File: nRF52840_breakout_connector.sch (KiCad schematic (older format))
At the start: 4 parts, among them J2 Conn_02x03_Odd_Even, J3 Conn_01x22, J4 Conn_01x16, J5 Conn_01x22

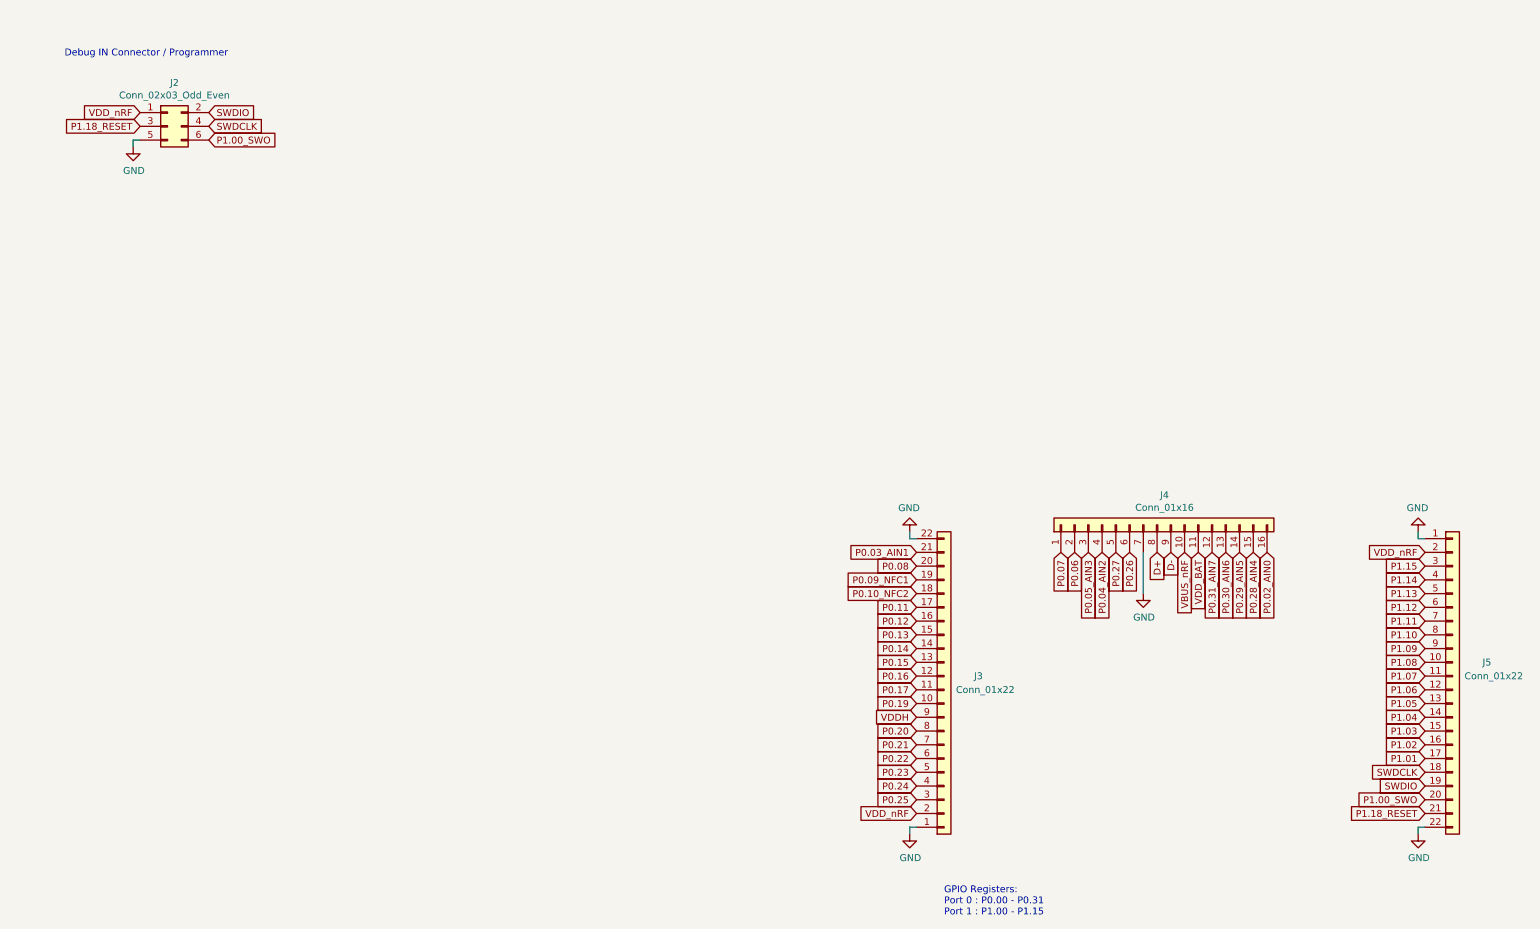
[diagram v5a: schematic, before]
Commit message: minor changes / switched from tag - 10pol debug connector
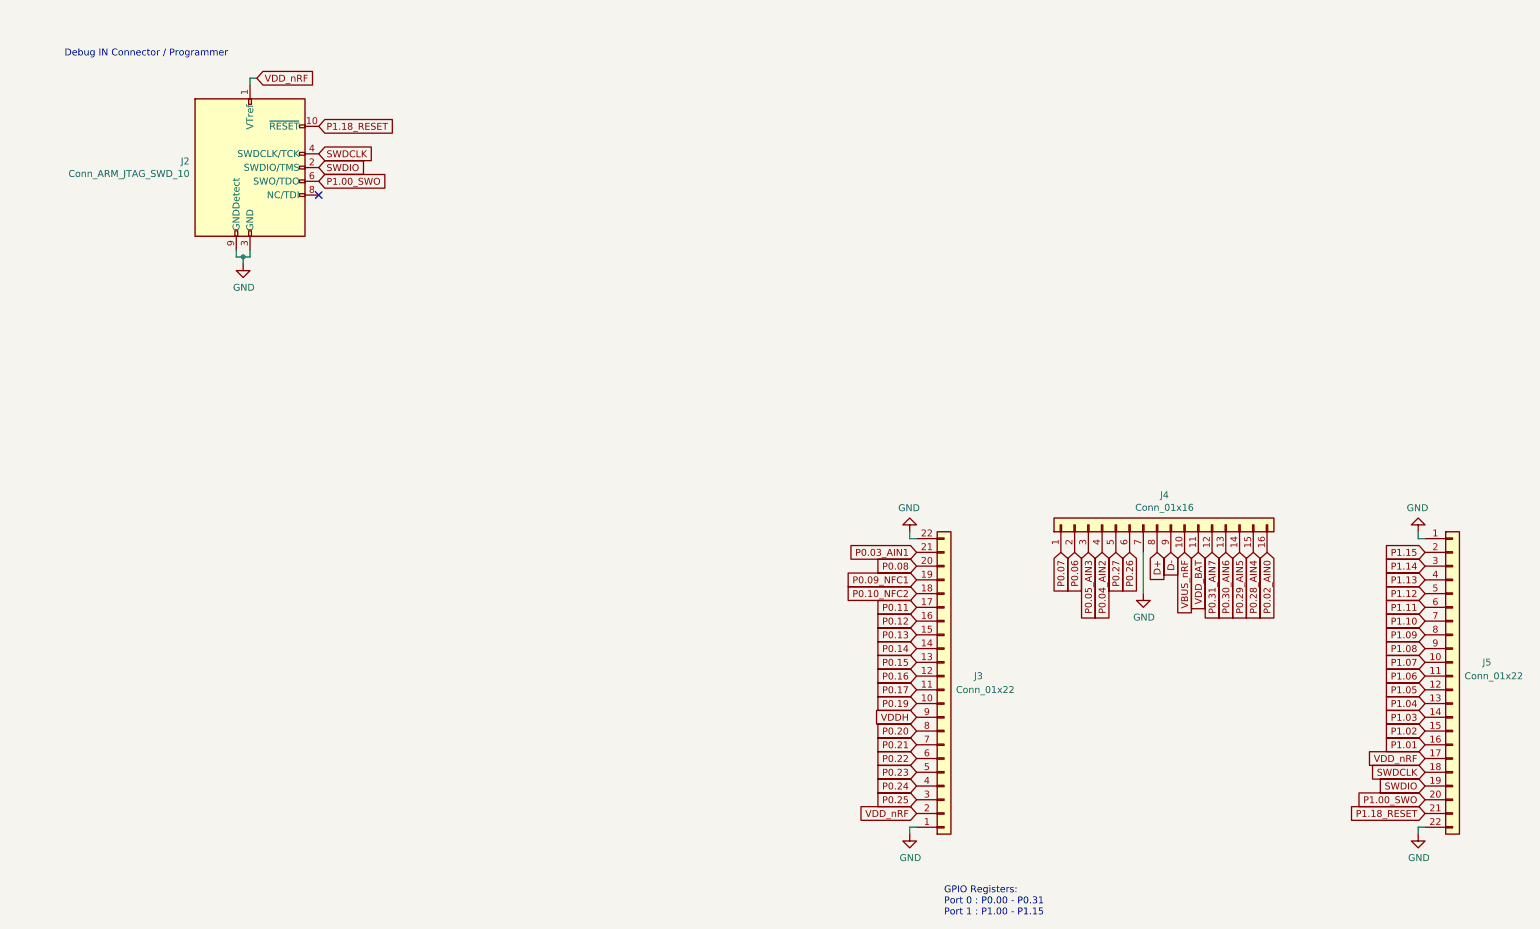
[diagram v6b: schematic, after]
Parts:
- removed J2: Conn_02x03_Odd_Even, Connector:Tag-Connect_TC2030-IDC-NL_2x03_P1.27mm_Vertical, symbol Connector_Generic:Conn_02x03_Odd_Even
- added J2: Conn_ARM_JTAG_SWD_10, Connector_PinHeader_1.27mm:PinHeader_2x05_P1.27mm_Vertical_SMD, symbol Connector:Conn_ARM_JTAG_SWD_10
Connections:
- net GND: now also J2.3 (GND), J2.5 (GND), J2.9 (GNDDetect)
- net P1.00_SWO: now also J2.6 (SWO/TDO)
- net P1.01: now also J5.16 (Pin_16); no longer J5.17 (Pin_17)
- net P1.02: now also J5.15 (Pin_15); no longer J5.16 (Pin_16)
- net P1.03: now also J5.14 (Pin_14); no longer J5.15 (Pin_15)
- net P1.04: now also J5.13 (Pin_13); no longer J5.14 (Pin_14)
- net P1.05: now also J5.12 (Pin_12); no longer J5.13 (Pin_13)
- net P1.06: now also J5.11 (Pin_11); no longer J5.12 (Pin_12)
- net P1.07: now also J5.10 (Pin_10); no longer J5.11 (Pin_11)
- net P1.08: now also J5.9 (Pin_9); no longer J5.10 (Pin_10)
- net P1.09: now also J5.8 (Pin_8); no longer J5.9 (Pin_9)
- net P1.10: now also J5.7 (Pin_7); no longer J5.8 (Pin_8)
- net P1.11: now also J5.6 (Pin_6); no longer J5.7 (Pin_7)
- net P1.12: now also J5.5 (Pin_5); no longer J5.6 (Pin_6)
- net P1.13: now also J5.4 (Pin_4); no longer J5.5 (Pin_5)
- net P1.14: now also J5.3 (Pin_3); no longer J5.4 (Pin_4)
- net P1.15: now also J5.2 (Pin_2); no longer J5.3 (Pin_3)
- net P1.18_RESET: now also J2.10 (~RESET~)
- net SWDCLK: now also J2.4 (SWDCLK/TCK)
- net SWDIO: now also J2.2 (SWDIO/TMS)
- net VDD_nRF: now also J5.17 (Pin_17), J2.1 (VTref); no longer J5.2 (Pin_2)
- no-connect marks 0 -> 1
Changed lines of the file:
@@
 Comment4 ""
 $EndDescr
-Text GLabel 1150 1000 0    50   Input ~ 0
-VDD_nRF
-$Comp
-L power:GND #PWR?
-U 1 1 5C9538B5
-P 1100 1250
-AR Path="/5C9538B5" Ref="#PWR?"  Part="1"
-AR Path="/5C94F379/5C9538B5" Ref="#PWR020"  Part="1"
-F 0 "#PWR020" H 1100 1000 50  0001 C CNN
-F 1 "GND" H 1105 1077 50  0000 C CNN
-F 2 "" H 1100 1250 50  0001 C CNN
-F 3 "" H 1100 1250 50  0001 C CNN
-	1    1100 1250
-	1    0    0    -1
-$EndComp
-Text GLabel 1650 1000 2    50   Input ~ 0
-SWDIO
-Text GLabel 1650 1100 2    50   Input ~ 0
-SWDCLK
 Text Notes 600  600  0    50   ~ 0
 Debug IN Connector / Programmer
@@
 Text GLabel 6800 4600 0    50   Input ~ 0
 P0.11
+Text GLabel 10500 4800 0    50   Input ~ 0
+P1.09
 Text GLabel 10500 4900 0    50   Input ~ 0
-P1.09
-Text GLabel 10500 5000 0    50   Input ~ 0
 P1.08
 Text GLabel 6800 4300 0    50   Input ~ 0
@@
 Text GLabel 10500 6000 0    50   Input ~ 0
 P1.00_SWO
-Text GLabel 10500 4600 0    50   Input ~ 0
+Text GLabel 10500 4500 0    50   Input ~ 0
 P1.12
-Text GLabel 10500 4500 0    50   Input ~ 0
+Text GLabel 10500 4400 0    50   Input ~ 0
 P1.13
-Text GLabel 10500 4400 0    50   Input ~ 0
+Text GLabel 10500 4300 0    50   Input ~ 0
 P1.14
-Text GLabel 10500 4300 0    50   Input ~ 0
+Text GLabel 10500 4200 0    50   Input ~ 0
 P1.15
 Text GLabel 6800 4200 0    50   Input ~ 0
@@
 Text GLabel 8950 4200 3    50   Input ~ 0
 P0.31_AIN7
-Text GLabel 10500 4800 0    50   Input ~ 0
+Text GLabel 10500 4700 0    50   Input ~ 0
 P1.10
-Text GLabel 10500 4700 0    50   Input ~ 0
+Text GLabel 10500 4600 0    50   Input ~ 0
 P1.11
 Text GLabel 6800 4500 0    50   Input ~ 0
@@
 Text GLabel 10500 5800 0    50   Input ~ 0
 SWDCLK
-Text GLabel 10500 5700 0    50   Input ~ 0
+Text GLabel 10500 5600 0    50   Input ~ 0
 P1.01
-Text GLabel 10500 5600 0    50   Input ~ 0
+Text GLabel 10500 5500 0    50   Input ~ 0
 P1.02
-Text GLabel 10500 5500 0    50   Input ~ 0
+Text GLabel 10500 5400 0    50   Input ~ 0
 P1.03
-Text GLabel 10500 5400 0    50   Input ~ 0
+Text GLabel 10500 5300 0    50   Input ~ 0
 P1.04
-Text GLabel 10500 5300 0    50   Input ~ 0
+Text GLabel 10500 5200 0    50   Input ~ 0
 P1.05
-Text GLabel 10500 5200 0    50   Input ~ 0
+Text GLabel 10500 5100 0    50   Input ~ 0
 P1.06
-Text GLabel 10500 5100 0    50   Input ~ 0
+Text GLabel 10500 5000 0    50   Input ~ 0
 P1.07
 Text GLabel 8850 4200 3    50   Input ~ 0
@@
 Wire Wire Line
 	6750 6200 6800 6200
-Text GLabel 10500 4200 0    50   Input ~ 0
+Text GLabel 10500 5700 0    50   Input ~ 0
 VDD_nRF
 $Comp
@@
 $EndComp
 $Comp
-L Connector_Generic:Conn_02x03_Odd_Even J2
-U 1 1 5CC7EB10
-P 1350 1100
-F 0 "J2" H 1400 1417 50  0000 C CNN
-F 1 "Conn_02x03_Odd_Even" H 1400 1326 50  0000 C CNN
-F 2 "Connector:Tag-Connect_TC2030-IDC-NL_2x03_P1.27mm_Vertical" H 1350 1100 50  0001 C CNN
-F 3 "~" H 1350 1100 50  0001 C CNN
-	1    1350 1100
-	1    0    0    -1
-$EndComp
-Text GLabel 1650 1200 2    50   Input ~ 0
+L Connector:Conn_ARM_JTAG_SWD_10 J2
+U 1 1 5CCC0F70
+P 1950 1400
+F 0 "J2" H 1510 1446 50  0000 R CNN
+F 1 "Conn_ARM_JTAG_SWD_10" H 1510 1355 50  0000 R CNN
+F 2 "Connector_PinHeader_1.27mm:PinHeader_2x05_P1.27mm_Vertical_SMD" H 1950 1400 50  0001 C CNN
+F 3 "http://infocenter.arm.com/help/topic/com.arm.doc.ddi0314h/DDI0314H_coresight_components_trm.pdf" V 1600 150 50  0001 C CNN
+	1    1950 1400
+	1    0    0    -1
+$EndComp
+Text GLabel 2450 1100 2    50   Input ~ 0
+P1.18_RESET
+Text GLabel 2450 1400 2    50   Input ~ 0
+SWDIO
+Text GLabel 2450 1300 2    50   Input ~ 0
+SWDCLK
+Text GLabel 2450 1500 2    50   Input ~ 0
 P1.00_SWO
-Text GLabel 1150 1100 0    50   Input ~ 0
-P1.18_RESET
-Wire Wire Line
-	1150 1200 1100 1200
-Wire Wire Line
-	1100 1200 1100 1250
+NoConn ~ 2450 1600
+$Comp
+L power:GND #PWR?
+U 1 1 5CCC1128
+P 1900 2100
+AR Path="/5CCC1128" Ref="#PWR?"  Part="1"
+AR Path="/5C94F379/5CCC1128" Ref="#PWR0123"  Part="1"
+F 0 "#PWR0123" H 1900 1850 50  0001 C CNN
+F 1 "GND" H 1905 1927 50  0000 C CNN
+F 2 "" H 1900 2100 50  0001 C CNN
+F 3 "" H 1900 2100 50  0001 C CNN
+	1    1900 2100
+	1    0    0    -1
+$EndComp
+Wire Wire Line
+	1850 2000 1850 2050
+Wire Wire Line
+	1850 2050 1900 2050
+Wire Wire Line
+	1950 2050 1950 2000
+Wire Wire Line
+	1900 2050 1900 2100
+Connection ~ 1900 2050
+Wire Wire Line
+	1900 2050 1950 2050
+Text GLabel 2000 750  2    50   Input ~ 0
+VDD_nRF
+Wire Wire Line
+	2000 750  1950 750
+Wire Wire Line
+	1950 750  1950 800
 $EndSCHEMATC

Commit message: layout / added part details etc
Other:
- moved on the sheet: J3, J4, J5

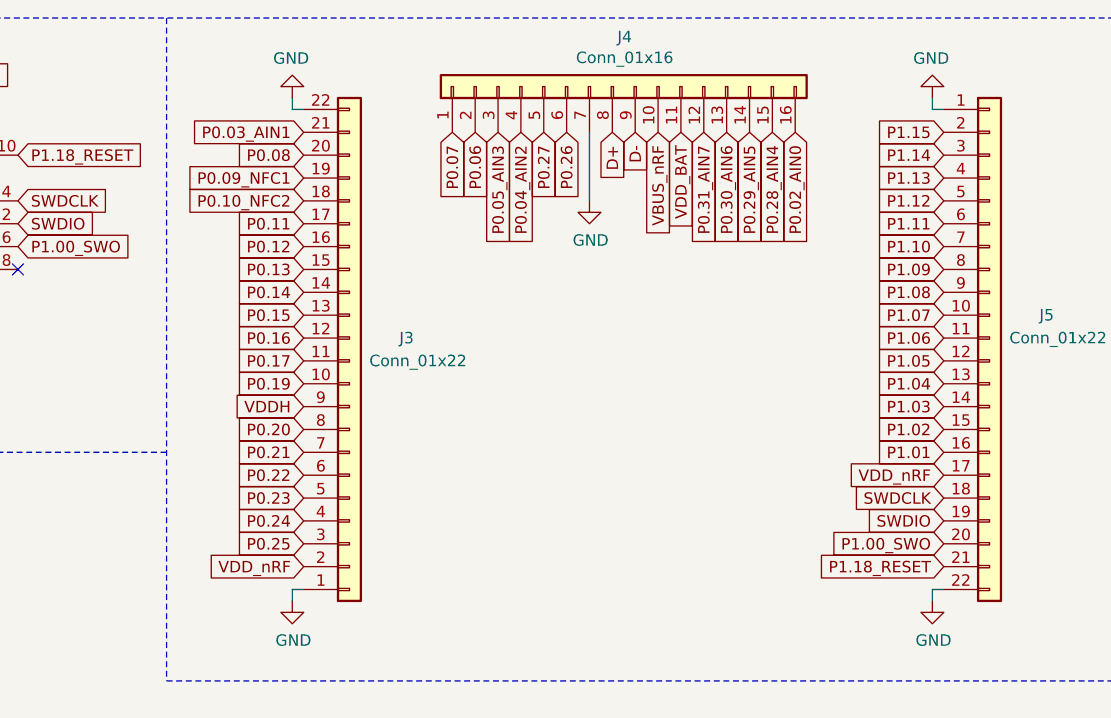
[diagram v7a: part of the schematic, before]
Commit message: 2 layer som version
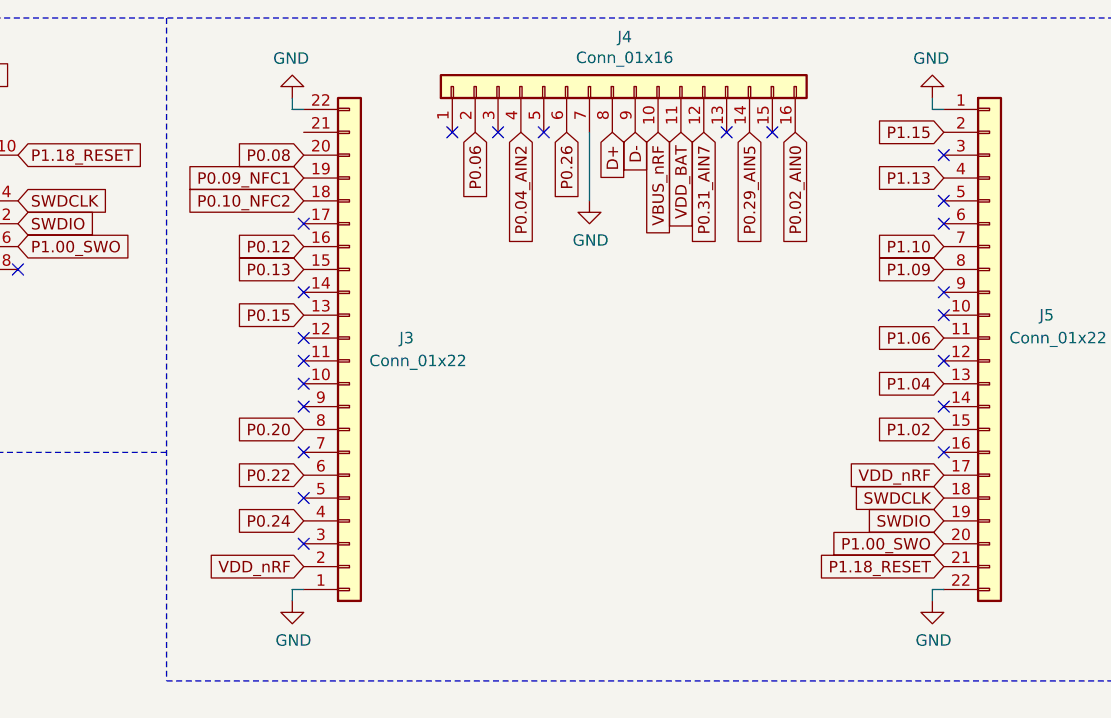
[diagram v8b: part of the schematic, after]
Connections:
- net P0.03_AIN1: no longer names the net of J3.21 (Pin_21)
- net P0.05_AIN3: no longer names the net of J4.3 (Pin_3)
- net P0.07: no longer names the net of J4.1 (Pin_1)
- net P0.11: no longer names the net of J3.17 (Pin_17)
- net P0.14: no longer names the net of J3.14 (Pin_14)
- net P0.16: no longer names the net of J3.12 (Pin_12)
- net P0.17: no longer names the net of J3.11 (Pin_11)
- net P0.19: no longer names the net of J3.10 (Pin_10)
- net P0.21: no longer names the net of J3.7 (Pin_7)
- net P0.23: no longer names the net of J3.5 (Pin_5)
- net P0.25: no longer names the net of J3.3 (Pin_3)
- net P0.27: no longer names the net of J4.5 (Pin_5)
- net P0.28_AIN4: no longer names the net of J4.15 (Pin_15)
- net P0.30_AIN6: no longer names the net of J4.13 (Pin_13)
- net P1.01: no longer names the net of J5.16 (Pin_16)
- net P1.03: no longer names the net of J5.14 (Pin_14)
- net P1.05: no longer names the net of J5.12 (Pin_12)
- net P1.07: no longer names the net of J5.10 (Pin_10)
- net P1.08: no longer names the net of J5.9 (Pin_9)
- net P1.11: no longer names the net of J5.6 (Pin_6)
- net P1.12: no longer names the net of J5.5 (Pin_5)
- net P1.14: no longer names the net of J5.3 (Pin_3)
- net VDDH: no longer names the net of J3.9 (Pin_9)
- no-connect marks 1 -> 23
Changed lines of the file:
@@
 EESchema Schematic File Version 4
 LIBS:nRF52840_breakout-cache
-EELAYER 26 0
+EELAYER 29 0
 EELAYER END
 $Descr A4 11693 8268
 encoding utf-8
-Sheet 2 4
+Sheet 2 3
 Title "nRF52840_breakout"
 Date "2019-03-22"
@@
 Text GLabel 3700 1500 0    50   Input ~ 0
 P0.12
-Text GLabel 3700 1400 0    50   Input ~ 0
-P0.11
 Text GLabel 6500 1600 0    50   Input ~ 0
 P1.09
-Text GLabel 6500 1700 0    50   Input ~ 0
-P1.08
 Text GLabel 3700 1100 0    50   Input ~ 0
 P0.08
-Text GLabel 4350 1000 3    50   Input ~ 0
-P0.07
 Text GLabel 4450 1000 3    50   Input ~ 0
 P0.06
-Text GLabel 4550 1000 3    50   Input ~ 0
-P0.05_AIN3
 Text GLabel 4650 1000 3    50   Input ~ 0
 P0.04_AIN2
-Text GLabel 4750 1000 3    50   Input ~ 0
-P0.27
 Text GLabel 4850 1000 3    50   Input ~ 0
 P0.26
 Text GLabel 6500 2900 0    50   Input ~ 0
 P1.18_RESET
-Text GLabel 3700 2000 0    50   Input ~ 0
-P0.17
-Text GLabel 3700 1900 0    50   Input ~ 0
-P0.16
 Text GLabel 3700 1800 0    50   Input ~ 0
 P0.15
-Text GLabel 3700 1700 0    50   Input ~ 0
-P0.14
-Text GLabel 3700 1600 0    50   Input ~ 0
-P0.13
 Text GLabel 5050 1000 3    50   Input ~ 0
 D+
@@
 Text GLabel 3700 2300 0    50   Input ~ 0
 P0.20
-Text GLabel 3700 2100 0    50   Input ~ 0
-P0.19
-Text GLabel 3700 2400 0    50   Input ~ 0
-P0.21
-Text GLabel 3700 2600 0    50   Input ~ 0
-P0.23
 Text GLabel 3700 2500 0    50   Input ~ 0
 P0.22
 Text GLabel 3700 2700 0    50   Input ~ 0
 P0.24
-Text GLabel 3700 2800 0    50   Input ~ 0
-P0.25
 Text GLabel 6500 2800 0    50   Input ~ 0
 P1.00_SWO
-Text GLabel 6500 1300 0    50   Input ~ 0
-P1.12
 Text GLabel 6500 1200 0    50   Input ~ 0
 P1.13
-Text GLabel 6500 1100 0    50   Input ~ 0
-P1.14
 Text GLabel 6500 1000 0    50   Input ~ 0
 P1.15
-Text GLabel 3700 1000 0    50   Input ~ 0
-P0.03_AIN1
 Text GLabel 5850 1000 3    50   Input ~ 0
 P0.02_AIN0
-Text GLabel 5750 1000 3    50   Input ~ 0
-P0.28_AIN4
 Text GLabel 5650 1000 3    50   Input ~ 0
 P0.29_AIN5
-Text GLabel 5550 1000 3    50   Input ~ 0
-P0.30_AIN6
 Text GLabel 5450 1000 3    50   Input ~ 0
 P0.31_AIN7
 Text GLabel 6500 1500 0    50   Input ~ 0
 P1.10
-Text GLabel 6500 1400 0    50   Input ~ 0
-P1.11
 Text GLabel 3700 1300 0    50   Input ~ 0
 P0.10_NFC2
@@
 Text GLabel 6500 2600 0    50   Input ~ 0
 SWDCLK
-Text GLabel 6500 2400 0    50   Input ~ 0
-P1.01
 Text GLabel 6500 2300 0    50   Input ~ 0
 P1.02
-Text GLabel 6500 2200 0    50   Input ~ 0
-P1.03
 Text GLabel 6500 2100 0    50   Input ~ 0
 P1.04
-Text GLabel 6500 2000 0    50   Input ~ 0
-P1.05
 Text GLabel 6500 1900 0    50   Input ~ 0
 P1.06
-Text GLabel 6500 1800 0    50   Input ~ 0
-P1.07
 Text GLabel 5350 1000 3    50   Input ~ 0
 VDD_BAT
@@
 Wire Wire Line
 	4950 1300 4950 1000
-Text GLabel 3700 2200 0    50   Input ~ 0
-VDDH
 $Comp
 L Connector_Generic:Conn_01x22 J3
@@
 Wire Notes Line
 	3100 500  3100 3400
+NoConn ~ 3700 2200
+NoConn ~ 3700 2100
+NoConn ~ 3700 2000
+Text GLabel 3700 1600 0    50   Input ~ 0
+P0.13
+NoConn ~ 3700 1900
+NoConn ~ 3700 1700
+NoConn ~ 3700 1400
+NoConn ~ 6500 1700
+NoConn ~ 6500 1100
+NoConn ~ 4350 1000
+NoConn ~ 4550 1000
+NoConn ~ 4750 1000
+NoConn ~ 5550 1000
+NoConn ~ 5750 1000
+NoConn ~ 6500 1300
+NoConn ~ 6500 1400
+NoConn ~ 6500 1800
+NoConn ~ 6500 2000
+NoConn ~ 6500 2200
+NoConn ~ 6500 2400
+NoConn ~ 3700 2800
+NoConn ~ 3700 2600
+NoConn ~ 3700 2400
 $EndSCHEMATC
